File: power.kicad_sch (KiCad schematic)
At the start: 147 parts, among them Q10 SI7613DN-T1-GE3, Q2 BC817-25W, Q3 DZDH0401DW, Q4 DZDH0401DW, Q5 SI7613DN-T1-GE3, Q6 SI7613DN-T1-GE3, Q7 BC817-25W, Q8 BC817-25W, Q9 SI7613DN-T1-GE3, U1 LT8350RV#PBF, U10 LM3881MME_NOPB, U2 MP2386GG, U3 TPS65983BAZBHR, U9 LM1117MP-3.3_NOPB

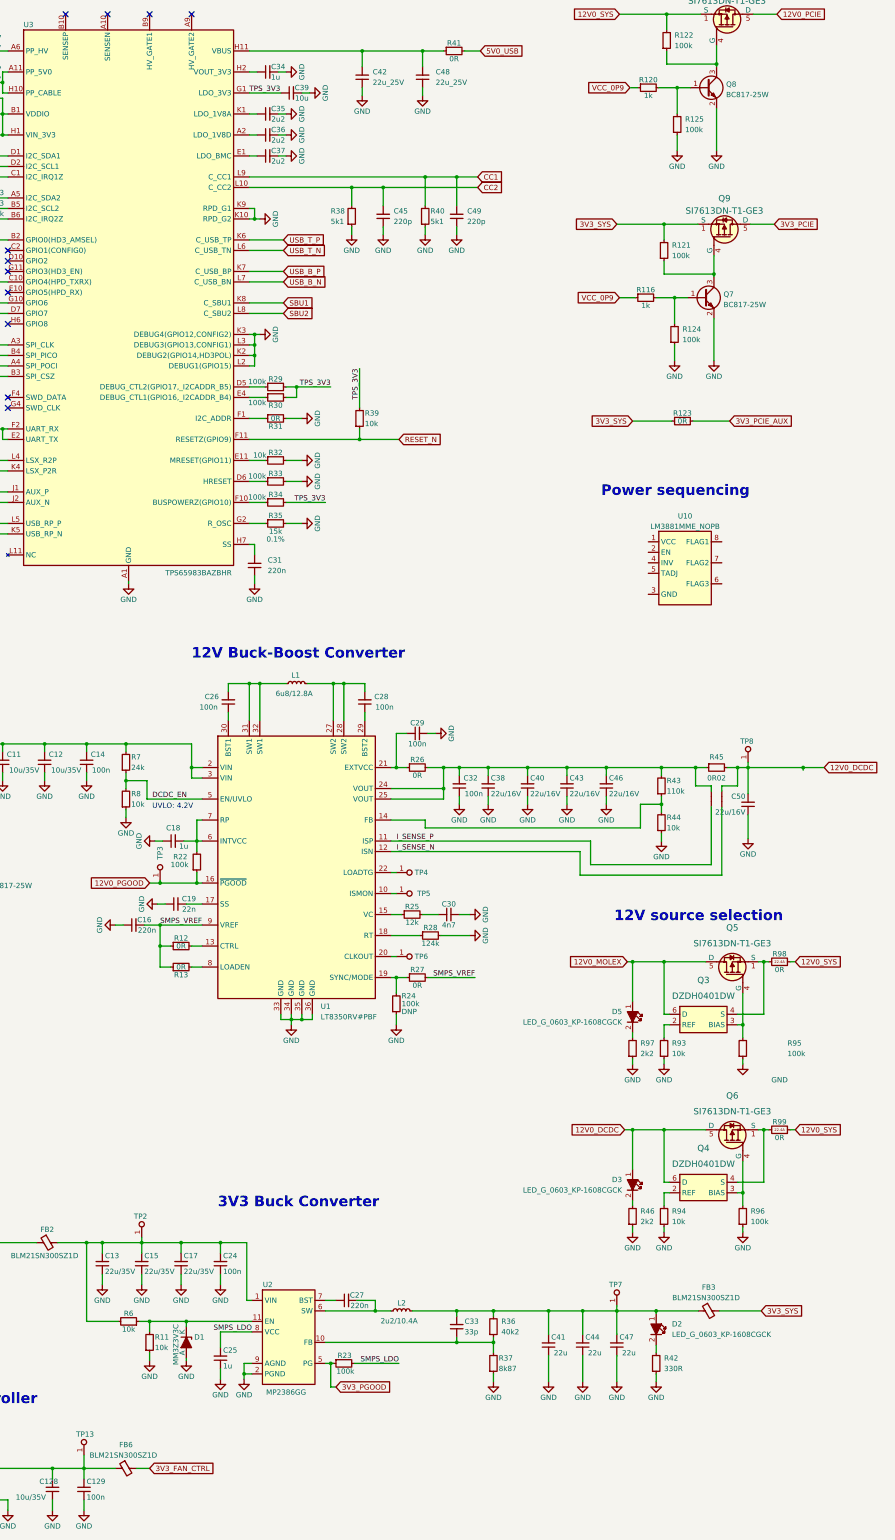
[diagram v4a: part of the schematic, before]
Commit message: Added optional power sequencer for PCIe device
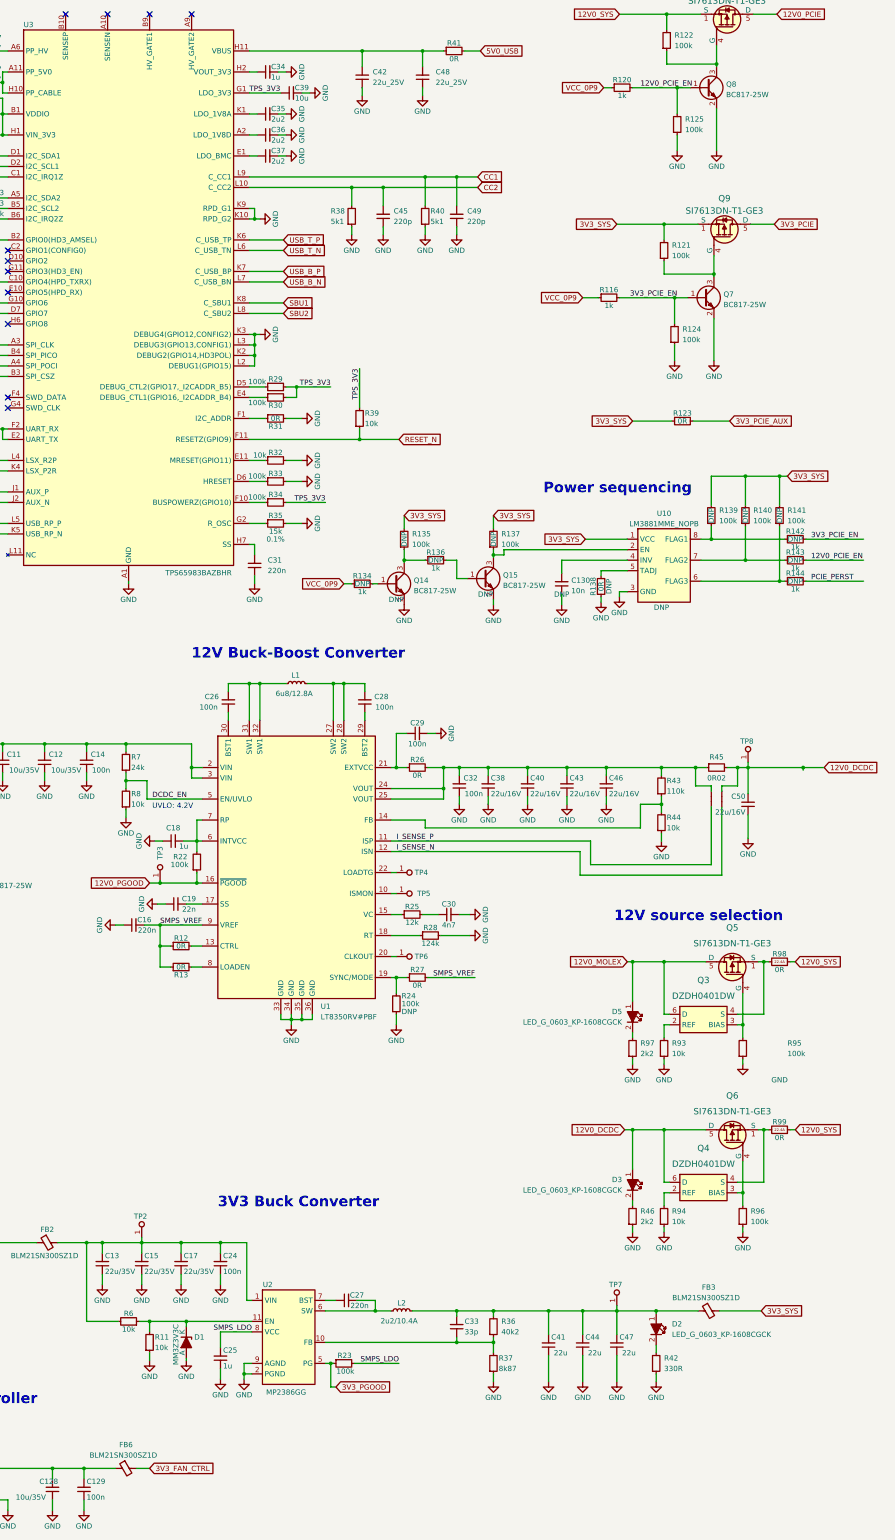
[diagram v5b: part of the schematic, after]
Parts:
- removed TP13: TP_1mm_SMD, antmicro-footprints:Testpoint_smd_1mm, symbol antmicroTestPoints:TP_1mm_SMD
- added C130: C_10n_0402, antmicro-footprints:C_0402_1005Metric, symbol antmicroCapacitors0402:C_10n_0402
- added Q14, Q15: BC817-25W, antmicro-footprints:SOT-323, symbol antmicroTransistorsBipolarSingle:BC817-25W
- added R134, R136, R142, R143, R144: R_1k_0402, antmicro-footprints:R_0402_1005Metric, symbol antmicroResistors0402:R_1k_0402
- added R135, R137, R139, R140, R141: R_100k_0402, antmicro-footprints:R_0402_1005Metric, symbol antmicroResistors0402:R_100k_0402
- added R138: R_0R_0402, antmicro-footprints:R_0402_1005Metric, symbol antmicroResistors0402:R_0R_0402
- U10: DNP (none) -> DNP
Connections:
- net 3V3_SYS: now also U10.1 (VCC), R135.2, R137.2, R139.2, R140.2, R141.2
- net GND: now also U10.3 (GND), C130.1, Q14.2 (E), Q15.2 (E), R138.1
- net VCC_0P9: now also R134.1
- net 3V3_PCIE_EN: now reaches Q7.1 (B), R116.2, R124.2
- net 3V3_PCIE_EN: now also R142.2
- net 12V0_PCIE_EN: now reaches Q8.1 (B), R120.2, R125.2
- net 12V0_PCIE_EN: now also R143.2
- net at U10.2 (EN): now also Q15.3 (C), R137.1
- net at U10.4 (INV): now also C130.2
- net at U10.5 (TADJ): now also R138.2
- net at U10.6 (FLAG3): now also R141.1, R144.1
- net at U10.7 (FLAG2): now also R140.1, R143.1
- net at U10.8 (FLAG1): now also R139.1, R142.1
- new net: Q14.1 (B), R134.2
- new net: Q14.3 (C), R135.1, R136.1
- new net: Q15.1 (B), R136.2
- new net PCIE_PERST: R144.2
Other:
- moved on the sheet: R116, R120, U10

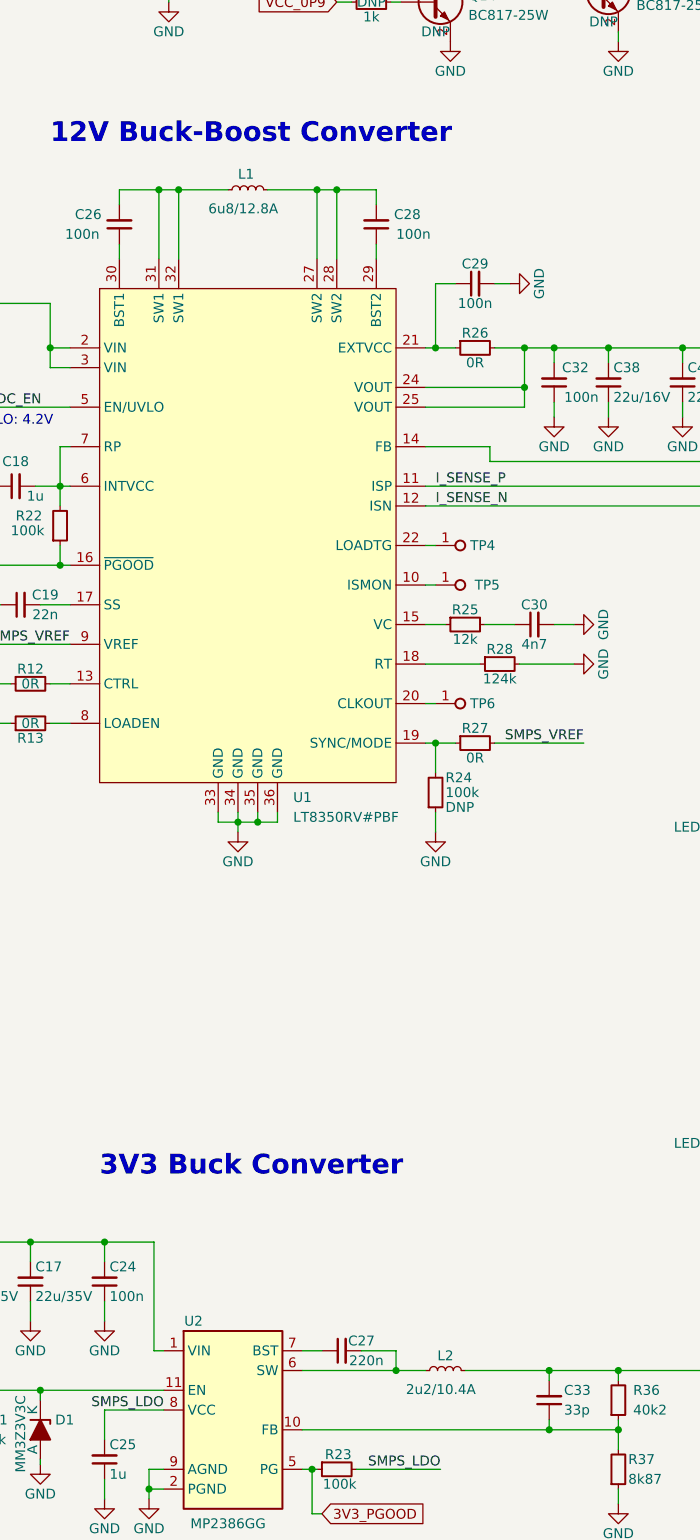
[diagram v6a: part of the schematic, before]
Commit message: [#49762] Fix missing 3D models
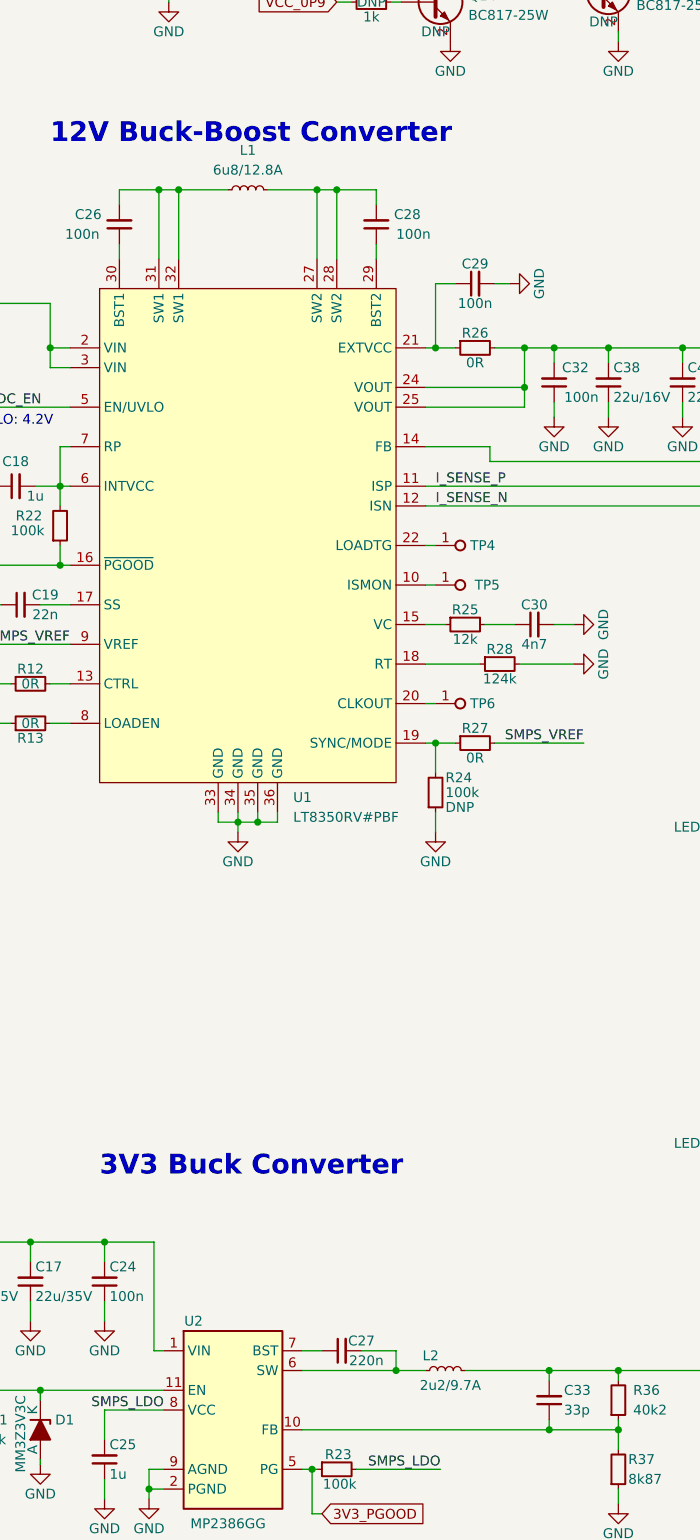
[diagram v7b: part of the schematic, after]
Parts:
- removed L1: L_6u8_12.8A_XAL7070, antmicro-footprints:L_Coilcraft_XAL7070, symbol antmicroFixedInductors:L_6u8_12.8A_XAL7070
- removed L2: L_2u2_10.4A_XAL5030, antmicro-footprints:L_Coilcraft_XAL5030, symbol antmicroFixedInductors:L_2u2_10.4A_XAL5030
- added L1: L_6u8_12.8A_Coilcraft-XAL7070, antmicro-footprints:L_Coilcraft-XAL7070, symbol antmicroFixedInductors:L_6u8_12.8A_Coilcraft-XAL7070
- added L2: L_2u2_9.7A_Coilcraft-XAL5030, antmicro-footprints:L_Coilcraft-XAL5030, symbol antmicroFixedInductors:L_2u2_9.7A_Coilcraft-XAL5030
- U1: footprint antmicro-footprints:LT8350 -> antmicro-footprints:QFN-32-4EP_4x6mm_P0.5mm
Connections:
- net at C27.2, U2.6 (SW): now also L2.1
- net at C33.2, C41.2, C44.2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: now also L2.2
- net at C28.2, U1.27 (SW2), U1.28 (SW2): now also L1.2
- net at C26.2, U1.31 (SW1), U1.32 (SW1): now also L1.1
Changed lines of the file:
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@@
       (effects (font (size 1.27 1.27)) (justify left))
     )
-    (property "Footprint" "antmicro-footprints:LT8350" (id 2) (at 201.295 255.905 0)
+    (property "Footprint" "antmicro-footprints:QFN-32-4EP_4x6mm_P0.5mm" (id 2) (at 201.295 255.905 0)
       (effects (font (size 1.27 1.27)) hide)
     )
@@
     (pin "2")
   )
-  (symbol (lib_id "antmicroFixedInductors:L_6u8_12.8A_XAL7070") (at 140.335 194.945 0) (unit 1)
-    (in_bom yes) (on_board yes)
-    (property "Reference" "L1" (id 0) (at 141.605 193.675 0)
-      (effects (font (size 1.27 1.27) (thickness 0.15)) (justify left bottom))
-    )
-    (property "Value" "L_6u8_12.8A_XAL7070" (id 1) (at 154.305 197.485 0)
-      (effects (font (size 1.27 1.27) (thickness 0.15)) (justify left bottom) hide)
-    )
-    (property "Footprint" "antmicro-footprints:L_Coilcraft_XAL7070" (id 2) (at 154.305 202.565 0)
-      (effects (font (size 1.27 1.27) (thickness 0.15)) (justify left bottom) hide)
-    )
-    (property "Datasheet" "https://www.coilcraft.com/en-us/products/power/shielded-inductors/molded-inductor/xal/xal7070/xal7070-682" (id 3) (at 154.305 205.105 0)
-      (effects (font (size 1.27 1.27) (thickness 0.15)) (justify left bottom) hide)
-    )
-    (property "Val" "6u8/12.8A" (id 4) (at 137.795 198.12 0)
-      (effects (font (size 1.27 1.27) (thickness 0.15)) (justify left bottom))
-    )
-    (property "Manufacturer" "Coilcraft" (id 5) (at 154.305 207.645 0)
-      (effects (font (size 1.27 1.27) (thickness 0.15)) (justify left bottom) hide)
-    )
-    (property "MPN" "XAL7070-682MEC" (id 6) (at 154.305 210.185 0)
-      (effects (font (size 1.27 1.27) (thickness 0.15)) (justify left bottom) hide)
-    )
-    (property "ISat" "12.8" (id 7) (at 154.305 211.455 0)
-      (effects (font (size 1.27 1.27)) (justify left) hide)
-    )
-    (property "IMax" "9.2" (id 8) (at 154.305 215.265 0)
-      (effects (font (size 1.27 1.27) (thickness 0.15)) (justify left bottom) hide)
-    )
-    (property "Size" "7.7x8" (id 9) (at 154.305 217.805 0)
-      (effects (font (size 1.27 1.27) (thickness 0.15)) (justify left bottom) hide)
-    )
-    (property "License" "Apache-2.0" (id 11) (at 154.305 222.885 0)
-      (effects (font (size 1.27 1.27) (thickness 0.15)) (justify left bottom) hide)
-    )
-    (property "Author" "Antmicro" (id 12) (at 154.305 220.345 0)
-      (effects (font (size 1.27 1.27) (thickness 0.15)) (justify left bottom) hide)
-    )
-    (pin "1")
-    (pin "2")
-  )
   (symbol (lib_id "antmicropower:GND") (at 62.23 41.91 270) (unit 1)
     (in_bom yes) (on_board yes)
@@
     (pin "3")
   )
+  (symbol (lib_id "antmicroFixedInductors:L_2u2_9.7A_Coilcraft-XAL5030") (at 165.735 346.71 0) (unit 1)
+    (in_bom yes) (on_board yes)
+    (property "Reference" "L2" (id 0) (at 166.37 344.805 0)
+      (effects (font (size 1.27 1.27) (thickness 0.15)))
+    )
+    (property "Value" "L_2u2_9.7A_Coilcraft-XAL5030" (id 1) (at 179.705 349.25 0)
+      (effects (font (size 1.27 1.27) (thickness 0.15)) (justify left bottom) hide)
+    )
+    (property "Footprint" "antmicro-footprints:L_Coilcraft-XAL5030" (id 2) (at 179.705 354.33 0)
+      (effects (font (size 1.27 1.27) (thickness 0.15)) (justify left bottom) hide)
+    )
+    (property "Datasheet" "https://www.coilcraft.com/getmedia/49bc46c8-4b2c-45b9-9b6c-2eaa235ea698/xal50xx.pdf" (id 3) (at 179.705 356.87 0)
+      (effects (font (size 1.27 1.27) (thickness 0.15)) (justify left bottom) hide)
+    )
+    (property "Val" "2u2/9.7A" (id 4) (at 168.91 348.615 0)
+      (effects (font (size 1.27 1.27) (thickness 0.15)))
+    )
+    (property "Manufacturer" "Coilcraft" (id 5) (at 179.705 359.41 0)
+      (effects (font (size 1.27 1.27) (thickness 0.15)) (justify left bottom) hide)
+    )
+    (property "MPN" "XAL5030-222MEC" (id 6) (at 179.705 361.95 0)
+      (effects (font (size 1.27 1.27) (thickness 0.15)) (justify left bottom) hide)
+    )
+    (property "ISat" "9.2 A" (id 7) (at 179.705 363.22 0)
+      (effects (font (size 1.27 1.27)) (justify left) hide)
+    )
+    (property "IMax" "9.7 A" (id 8) (at 179.705 367.03 0)
+      (effects (font (size 1.27 1.27) (thickness 0.15)) (justify left bottom) hide)
+    )
+    (property "Size" "5.28x5.48" (id 9) (at 179.705 369.57 0)
+      (effects (font (size 1.27 1.27) (thickness 0.15)) (justify left bottom) hide)
+    )
+    (property "Author" "Antmicro" (id 10) (at 179.705 372.11 0)
+      (effects (font (size 1.27 1.27) (thickness 0.15)) (justify left bottom) hide)
+    )
+    (property "License" "Apache-2.0" (id 11) (at 179.705 374.65 0)
+      (effects (font (size 1.27 1.27) (thickness 0.15)) (justify left bottom) hide)
+    )
+    (pin "1")
+    (pin "2")
+  )
   (symbol (lib_id "antmicropower:GND") (at 132.715 170.815 0) (unit 1)
     (in_bom yes) (on_board yes)
@@
     (pin "2")
   )
-  (symbol (lib_id "antmicroFixedInductors:L_2u2_10.4A_XAL5030") (at 165.735 346.71 0) (unit 1)
-    (in_bom yes) (on_board yes)
-    (property "Reference" "L2" (id 0) (at 168.275 344.805 0)
-      (effects (font (size 1.27 1.27) (thickness 0.15)))
-    )
-    (property "Value" "L_2u2_10.4A_XAL5030" (id 1) (at 179.705 349.25 0)
-      (effects (font (size 1.27 1.27) (thickness 0.15)) (justify left bottom) hide)
-    )
-    (property "Footprint" "antmicro-footprints:L_Coilcraft_XAL5030" (id 2) (at 179.705 354.33 0)
-      (effects (font (size 1.27 1.27) (thickness 0.15)) (justify left bottom) hide)
-    )
-    (property "Datasheet" "https://www.mouser.pl/datasheet/2/597/xal50xx-270657.pdf" (id 3) (at 179.705 356.87 0)
-      (effects (font (size 1.27 1.27) (thickness 0.15)) (justify left bottom) hide)
-    )
-    (property "Val" "2u2/10.4A" (id 4) (at 163.195 349.885 0)
-      (effects (font (size 1.27 1.27) (thickness 0.15)) (justify left bottom))
-    )
-    (property "Manufacturer" "Coilcraft" (id 5) (at 179.705 359.41 0)
-      (effects (font (size 1.27 1.27) (thickness 0.15)) (justify left bottom) hide)
-    )
-    (property "MPN" "XAL5030-222MEC" (id 6) (at 179.705 361.95 0)
-      (effects (font (size 1.27 1.27) (thickness 0.15)) (justify left bottom) hide)
-    )
-    (property "ISat" "9.2" (id 7) (at 179.705 363.22 0)
-      (effects (font (size 1.27 1.27)) (justify left) hide)
-    )
-    (property "IMax" "9.7" (id 8) (at 179.705 367.03 0)
-      (effects (font (size 1.27 1.27) (thickness 0.15)) (justify left bottom) hide)
-    )
-    (property "Size" "5.28x5.48" (id 9) (at 179.705 369.57 0)
-      (effects (font (size 1.27 1.27) (thickness 0.15)) (justify left bottom) hide)
-    )
-    (property "License" "Apache-2.0" (id 11) (at 179.705 374.65 0)
-      (effects (font (size 1.27 1.27) (thickness 0.15)) (justify left bottom) hide)
-    )
-    (property "Author" "Antmicro" (id 12) (at 179.705 372.11 0)
-      (effects (font (size 1.27 1.27) (thickness 0.15)) (justify left bottom) hide)
-    )
-    (pin "1")
-    (pin "2")
-  )
   (symbol (lib_name "R_0R_0402_1") (lib_id "antmicroResistors0402:R_0R_0402") (at 135.255 130.81 0) (unit 1)
     (in_bom yes) (on_board yes)
@@
     (pin "1")
   )
+  (symbol (lib_id "antmicroFixedInductors:L_6u8_12.8A_Coilcraft-XAL7070") (at 140.335 194.945 0) (unit 1)
+    (in_bom yes) (on_board yes)
+    (property "Reference" "L1" (id 0) (at 142.875 189.865 0)
+      (effects (font (size 1.27 1.27) (thickness 0.15)))
+    )
+    (property "Value" "L_6u8_12.8A_Coilcraft-XAL7070" (id 1) (at 154.305 197.485 0)
+      (effects (font (size 1.27 1.27) (thickness 0.15)) (justify left bottom) hide)
+    )
+    (property "Footprint" "antmicro-footprints:L_Coilcraft-XAL7070" (id 2) (at 154.305 202.565 0)
+      (effects (font (size 1.27 1.27) (thickness 0.15)) (justify left bottom) hide)
+    )
+    (property "Datasheet" "https://www.coilcraft.com/en-us/products/power/shielded-inductors/molded-inductor/xal/xal7070/xal7070-682" (id 3) (at 154.305 205.105 0)
+      (effects (font (size 1.27 1.27) (thickness 0.15)) (justify left bottom) hide)
+    )
+    (property "Val" "6u8/12.8A" (id 4) (at 142.875 192.405 0)
+      (effects (font (size 1.27 1.27) (thickness 0.15)))
+    )
+    (property "Manufacturer" "Coilcraft" (id 5) (at 154.305 207.645 0)
+      (effects (font (size 1.27 1.27) (thickness 0.15)) (justify left bottom) hide)
+    )
+    (property "MPN" "XAL7070-682MEC" (id 6) (at 154.305 210.185 0)
+      (effects (font (size 1.27 1.27) (thickness 0.15)) (justify left bottom) hide)
+    )
+    (property "ISat" "12.8 A" (id 7) (at 154.305 211.455 0)
+      (effects (font (size 1.27 1.27)) (justify left) hide)
+    )
+    (property "IMax" "9.2 A" (id 8) (at 154.305 215.265 0)
+      (effects (font (size 1.27 1.27) (thickness 0.15)) (justify left bottom) hide)
+    )
+    (property "Size" "7.7x8" (id 9) (at 154.305 217.805 0)
+      (effects (font (size 1.27 1.27) (thickness 0.15)) (justify left bottom) hide)
+    )
+    (property "Author" "Antmicro" (id 10) (at 154.305 220.345 0)
+      (effects (font (size 1.27 1.27) (thickness 0.15)) (justify left bottom) hide)
+    )
+    (property "License" "Apache-2.0" (id 11) (at 154.305 222.885 0)
+      (effects (font (size 1.27 1.27) (thickness 0.15)) (justify left bottom) hide)
+    )
+    (pin "1")
+    (pin "2")
+  )
   (symbol (lib_id "antmicropower:GND") (at 158.75 52.705 0) (unit 1)
